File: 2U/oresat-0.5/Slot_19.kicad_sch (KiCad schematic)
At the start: 3 parts

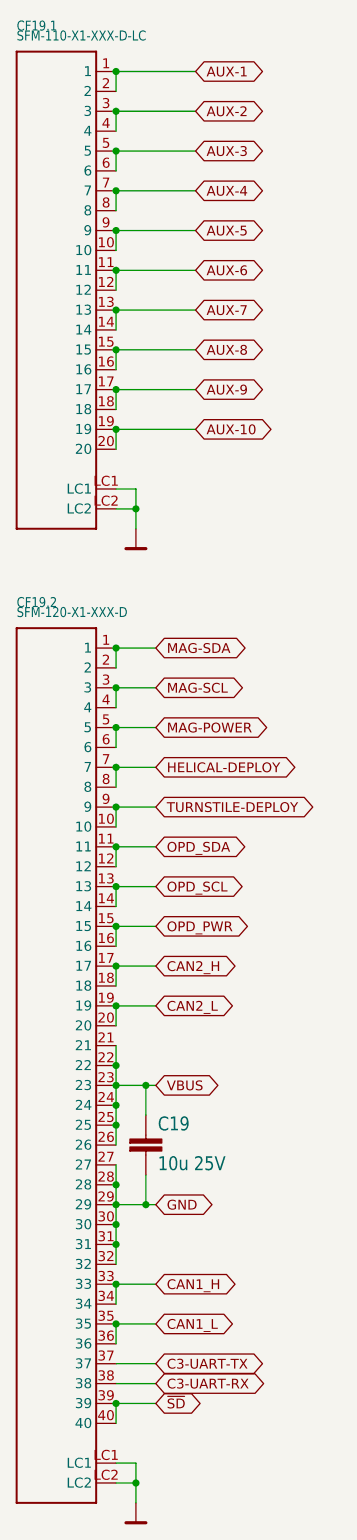
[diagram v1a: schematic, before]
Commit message: Fixed all (most) of the issues from Eagle imports
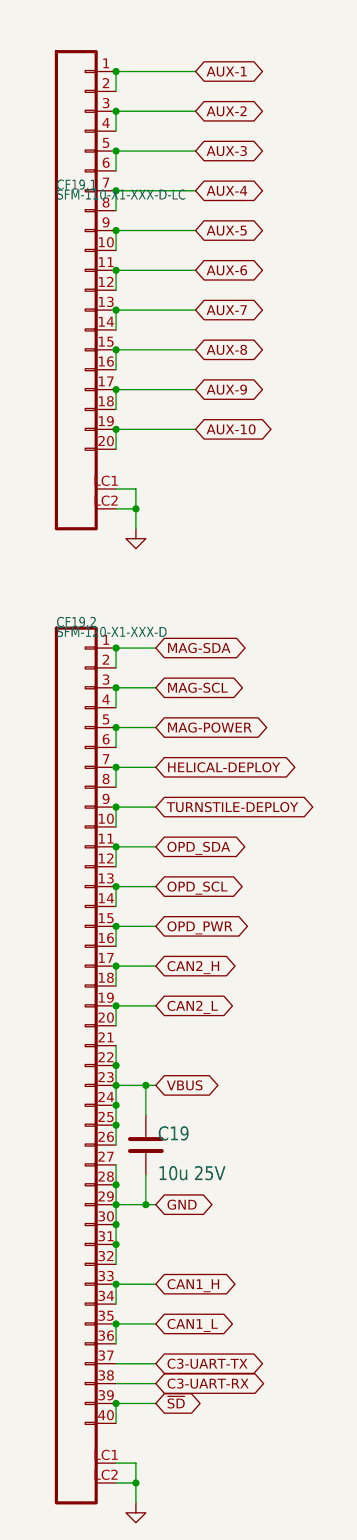
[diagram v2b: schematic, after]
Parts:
- C19: symbol oresat0-1u-backplane-eagle-import:C-EU1206-B -> Device:C
- CF19.1: symbol oresat-backplane-2u-eagle-import:SFM-110-X1-XXX-D-LC -> oresat-connectors:J-SAMTEC-TFM-110-01-L-D-RA
- CF19.2: symbol oresat-backplane-2u-eagle-import:SFM-120-X1-XXX-D -> oresat-connectors:J-SAMTEC-TFM-120-01-L-D-RA

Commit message: Moved entire schematic to single page
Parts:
- removed C19: 10u 25V, Capacitor_SMD:C_1206_3216Metric, symbol Device:C
- removed CF19.1: SFM-110-X1-XXX-D-LC, oresat-connectors:J-SAMTEC-CF-SFM-110-X1-XXX-D-LC, symbol oresat-connectors:J-SAMTEC-TFM-110-01-L-D-RA
- removed CF19.2: SFM-120-X1-XXX-D, oresat-connectors:J-SAMTEC-SFM-120-X1-XXX-D, symbol oresat-connectors:J-SAMTEC-TFM-120-01-L-D-RA
